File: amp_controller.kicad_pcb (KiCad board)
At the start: 4 copper layers, 62.3 x 61 mm, 50 parts, among them Q1 BC848, Q2 BC848, Q3 BC848, U1 RaspberryPi_Pico_W, U2 TSR_1-2450, U3 LT1175-5_SOT223, U4 LM4040DBZ-3, U6 EL3H7(C)(TA)-G, U7 MCP1700x-330xxTT, U8 LM2904

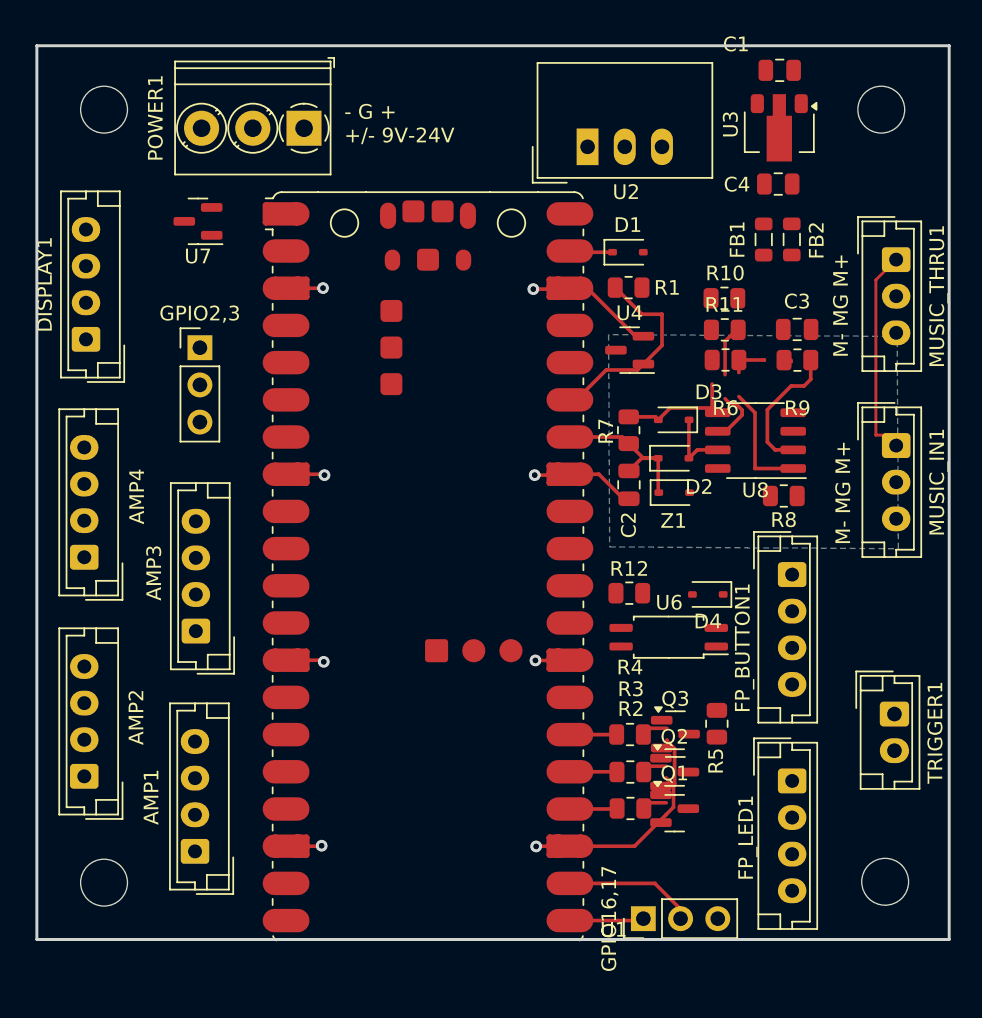
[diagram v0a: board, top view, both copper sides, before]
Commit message: passing DRC check, op amp input issue fixed
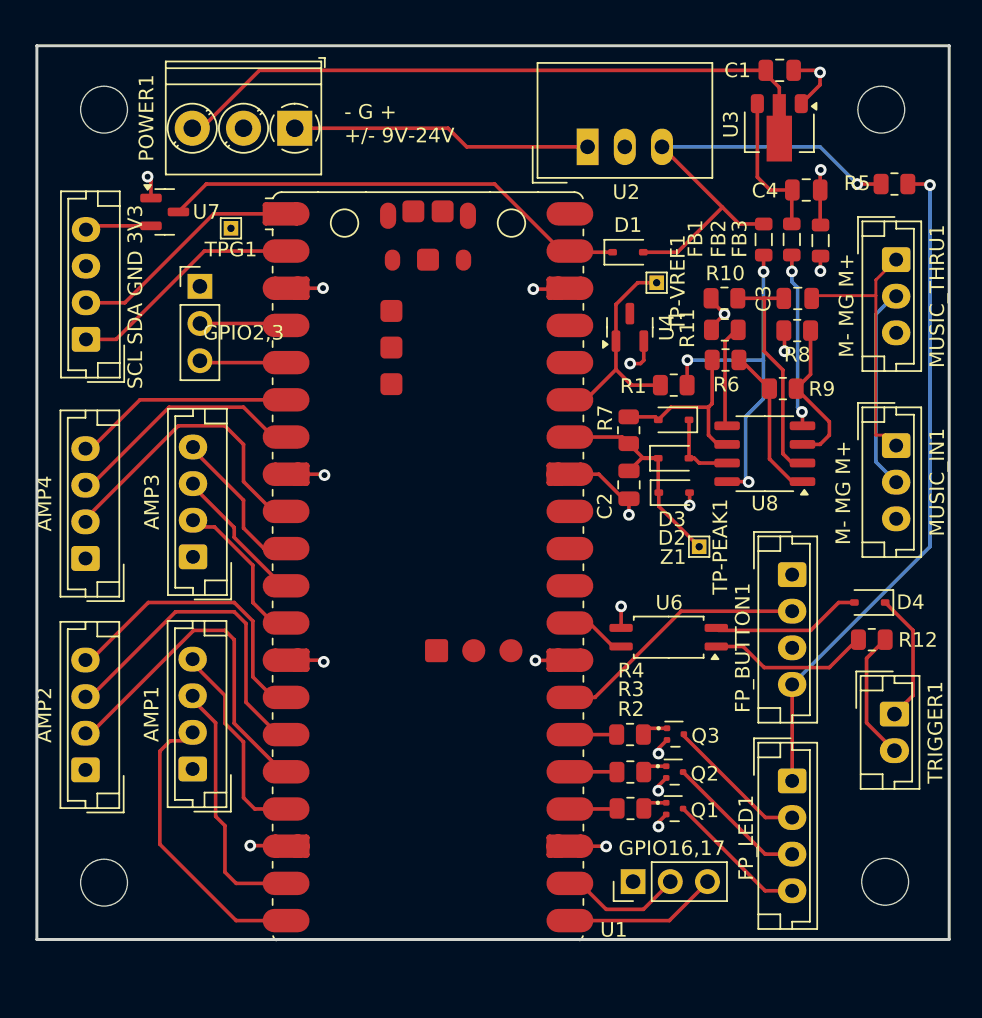
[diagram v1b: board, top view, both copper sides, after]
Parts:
- added FB3: FerriteBead, Inductor_SMD:L_0805_2012Metric, F.Cu at (159.9, 77.3)
- added TP-PEAK1: TestPoint, TestPoint:TestPoint_THTPad_1.0x1.0mm_Drill0.5mm, F.Cu at (151.6, 98.2)
- added TP-VREF1: TestPoint, TestPoint:TestPoint_THTPad_1.0x1.0mm_Drill0.5mm, F.Cu at (148.7, 80.2)
- added TPG1: TestPoint, TestPoint:TestPoint_THTPad_1.0x1.0mm_Drill0.5mm, F.Cu at (119.6, 76.4)
- Q1, Q2, Q3: footprint Package_TO_SOT_SMD:SOT-23 -> Package_TO_SOT_SMD:SOT-723
- moved R5 38.8 mm to (164.9, 73.4), turned to 0 degrees
- moved R12 16.9 mm to (163.4, 104.5), turned to 180 degrees
- moved R8 11.3 mm to (158.3, 83.4)
- moved D4 11.1 mm to (163.2, 102.0)
- moved R1 7.34 mm to (149.8, 87.1)
- moved AMP1 5.63 mm to (117.0, 113.4)
- moved AMP3 5.08 mm to (117.0, 98.9)
- moved GPIO2,3 4.19 mm to (117.5, 80.4)
- moved GPIO16,17 2.62 mm to (147.1, 121.0)
- moved U7 2.36 mm to (115.1, 75.3), turned to 0 degrees
- moved R9 2.18 mm to (157.3, 87.4)
- moved C3 2.12 mm to (158.3, 81.2)
- moved C4 1.96 mm to (158.9, 73.8)
- moved U4 1.56 mm to (146.8, 83.2), turned to 90 degrees
- moved U8 1.10 mm to (156.1, 91.8)
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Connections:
- C2 pad 2: GND -> AGND
- C3 pad 2: Net-(U8A-+) -> Net-(U8A--)
- GPIO16,17 pad 1: Net-(GPIO16,17-Pin_1) -> GND
- GPIO16,17 pad 3: GND -> Net-(GPIO16,17-Pin_3)
- R10 pad 1: Net-(U8A-+) -> Net-(U8A--)
- R10 pad 2: GND -> AGND
- R11 pad 1: Net-(U8B--) -> Net-(U8B-+)
- R11 pad 2: GND -> AGND
- R8 pad 1: Net-(U8A--) -> Net-(U8A-+)
- R8 pad 2: GND -> AGND
- R9 pad 1: Net-(U8A--) -> Net-(U8A-+)
- U1 pad 21: Net-(GPIO16,17-Pin_1) -> Net-(GPIO16,17-Pin_3)
- U1 pad 33: GND -> AGND
- U4 pad 2: GND -> AGND
- U7 pad 3: +5V -> VSYS
- U8 pad 5: Net-(D3-A) -> Net-(U8B-+)
- U8 pad 6: Net-(U8B--) -> Net-(D3-A)
- Z1 pad 2: GND -> AGND
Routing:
- net /DRV: track 0.00 -> 46.1 mm, vias 0 -> 1
- net /-18V: track 0.00 -> 42.9 mm
- net +5V: track 0.00 -> 31.8 mm, vias 0 -> 1
- net VSYS: track 3.75 -> 32.5 mm
- net /AMP2_CLIP: track 0.00 -> 25.0 mm
- net +5VA: track 0.00 -> 24.6 mm, vias 0 -> 3
- net /AMP2_FAULT: track 0.00 -> 23.8 mm
- net /AMP4_CLIP: track 0.00 -> 21.6 mm
- net /AMP2_RESET: track 0.00 -> 21.3 mm
- net /AMP1_CLIP: track 0.00 -> 20.8 mm
- net /+18V: track 0.00 -> 19.9 mm
- net /FP_BUTTON: track 0.00 -> 18.4 mm
- net /AMP4_FAULT: track 0.00 -> 17.7 mm
- net /AMP1_FAULT: track 0.00 -> 17.6 mm
- net /SDA: track 0.00 -> 17.0 mm
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- added copper zone on In1.Cu, net AGND
- removed copper zone on In2.Cu, net +5VA
- removed copper zone on B.Cu, net -5VA
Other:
- board text added: "SCL SDA GND 3V3"

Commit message: tweaked layout and music sense resistors
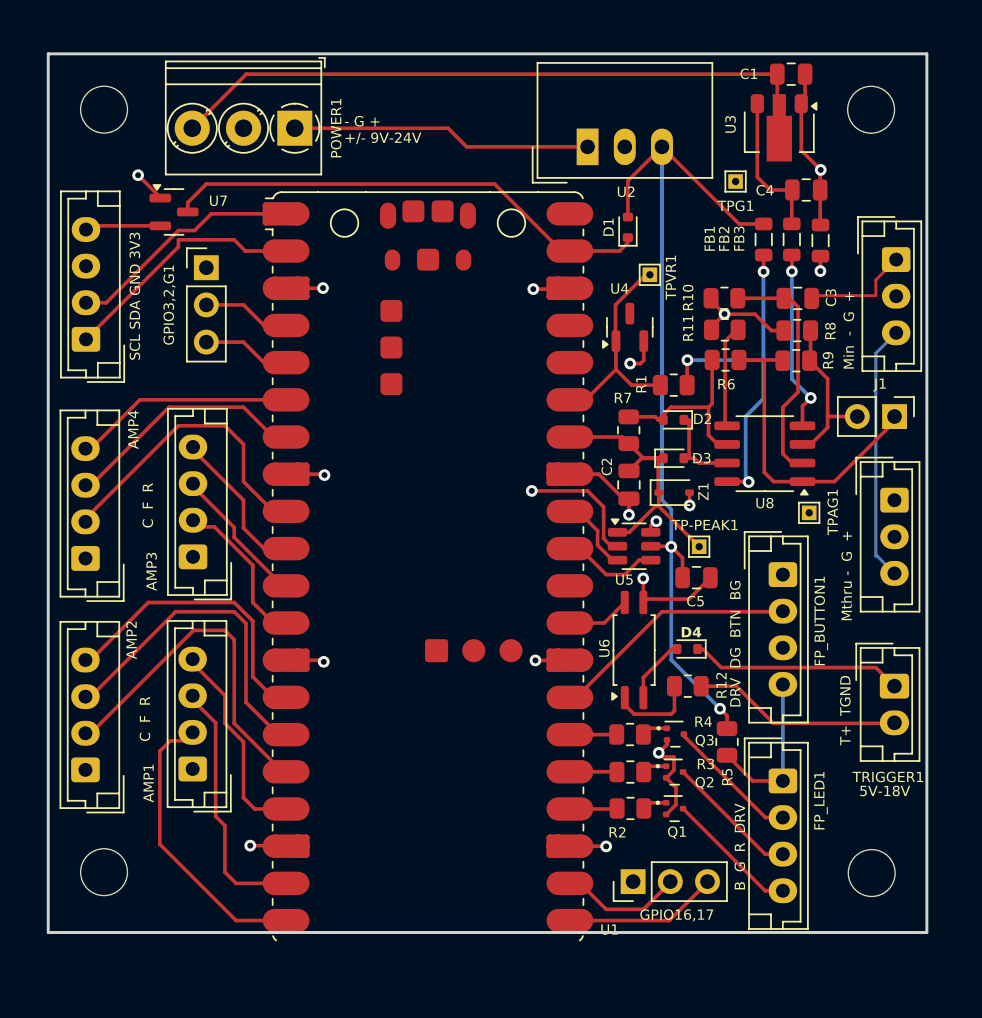
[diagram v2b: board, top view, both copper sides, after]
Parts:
- removed GPIO2,3: Conn_01x02_Pin, Connector_PinHeader_2.54mm:PinHeader_1x03_P2.54mm_Vertical
- removed TP-VREF1: TestPoint, TestPoint:TestPoint_THTPad_1.0x1.0mm_Drill0.5mm
- added C5: 1u, Capacitor_SMD:C_0805_2012Metric, F.Cu at (151.4, 100.3)
- added GPIO3,2,G1: Conn_01x02_Pin, Connector_PinHeader_2.54mm:PinHeader_1x03_P2.54mm_Vertical, F.Cu at (117.9, 79.1)
- added J1: Conn_01x02_Pin, Connector_PinHeader_2.54mm:PinHeader_1x02_P2.54mm_Vertical, F.Cu at (164.9, 89.3)
- added TPAG1: TestPoint, TestPoint:TestPoint_THTPad_1.0x1.0mm_Drill0.5mm, F.Cu at (159.1, 95.9)
- added TPVR1: TestPoint, TestPoint:TestPoint_THTPad_1.0x1.0mm_Drill0.5mm, F.Cu at (148.2, 79.6)
- added U5: ADS1110, Package_TO_SOT_SMD:SOT-23-6, F.Cu at (147.1, 98.1)
- D1, D2, D3, D4: value 1N5819WS -> D_Schottky; footprint Diode_SMD:D_SOD-323 -> Diode_SMD:D_SOD-523
- R10: value 90k -> 91k
- R6, R7: value 10k -> 1M
- R8: value 10k -> 100k
- R9: value 100k -> 1M
- moved R5 39.8 mm to (153.5, 111.5), turned to -90 degrees
- moved TPG1 34.6 mm to (154.1, 73.2)
- moved R12 13.0 mm to (150.8, 107.7)
- moved D4 12.9 mm to (150.8, 105.2)
- moved MUSIC_IN1 3.73 mm to (164.9, 95.0)
- moved U6 2.52 mm to (147.1, 105.2), turned to 90 degrees
- moved R9 2.11 mm to (158.2, 85.5)
- moved TRIGGER1 1.90 mm to (164.9, 107.7)
- moved D1 1.70 mm to (146.7, 76.4), turned to 90 degrees
- moved H4 1.09 mm to (163.4, 120.5)
- moved C1 0.83 mm to (157.9, 65.9)
- moved H2 0.71 mm to (110.9, 120.4)
- moved H3 0.69 mm to (163.3, 68.3)
- moved U7 0.64 mm to (115.7, 75.3)
- moved FP_BUTTON1 0.63 mm to (157.3, 100.1)
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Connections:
- net Net-(GPIO16,17-Pin_2) renamed /GPIO17
- net Net-(GPIO16,17-Pin_3) renamed /GPIO16
- U1 pad 31: unconnected-(U1-GPIO26_ADC0-Pad31) -> /I2C1_SDA
- U1 pad 32: unconnected-(U1-GPIO27_ADC1-Pad32) -> /I2C1_SCL
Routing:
- net /DRV: track 46.1 -> 11.1 mm, vias 1 -> 0
- net +5V: track 31.8 -> 60.0 mm, vias 1 -> 2
- net GND: track 29.9 -> 51.0 mm, vias 14 -> 12
- net Net-(J1-Pin_1): track 10.6 -> 22.0 mm
- net /I2C1_SDA: track 0.00 -> 7.47 mm
- net /M+: track 18.7 -> 25.0 mm
- net Net-(D4-A): track 10.3 -> 4.13 mm
- net /I2C1_SCL: track 0.00 -> 6.01 mm
- net Net-(TRIGGER1-Pin_2): track 8.89 -> 14.3 mm
- net Net-(D4-K): track 8.93 -> 14.1 mm
- net Net-(R12-Pad2): track 11.1 -> 5.92 mm
- net AGND: track 15.3 -> 19.5 mm
- net /M-: track 13.9 -> 17.6 mm
- net /MG: track 13.9 -> 17.6 mm
- net /PEAK: track 17.0 -> 20.5 mm
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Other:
- board size 62.3 x 61 mm -> 60 x 60 mm
- board text added: "5V-18V"
- board text added: "Amp module controller (c) Matt Clark 2023 Board 60mm x 60mm Mounting holes ... Input +-6.5VDC to +-36VDC"
- board text added: "B G R DRV"
- board text added: "C F R"
- board text added: "DRV DG BTN BG"
- board text added: "Min - G +"
- board text added: "Mthru - G +"
- board text added: "T+ TGND"
- board text removed: "Amp module controller (c) Matt Clark 2023"
- board text removed: "M- MG M+"
